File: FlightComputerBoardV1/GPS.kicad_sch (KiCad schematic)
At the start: 1 part

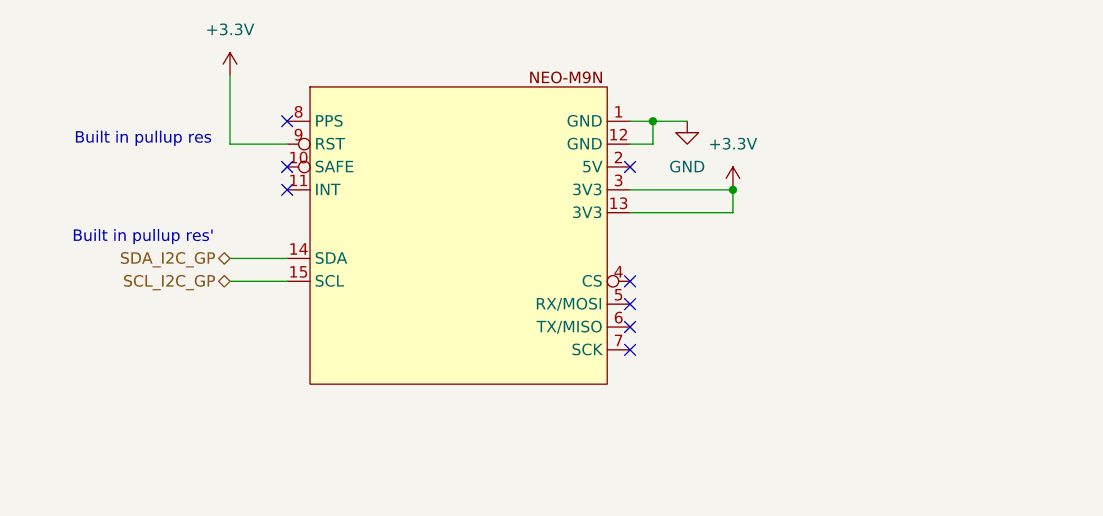
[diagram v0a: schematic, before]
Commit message: Test Points, BMP581
- Added I2C and other test points to schematic
- Added BMP581 symbol, footprint, and schematic on Peripherals sheet
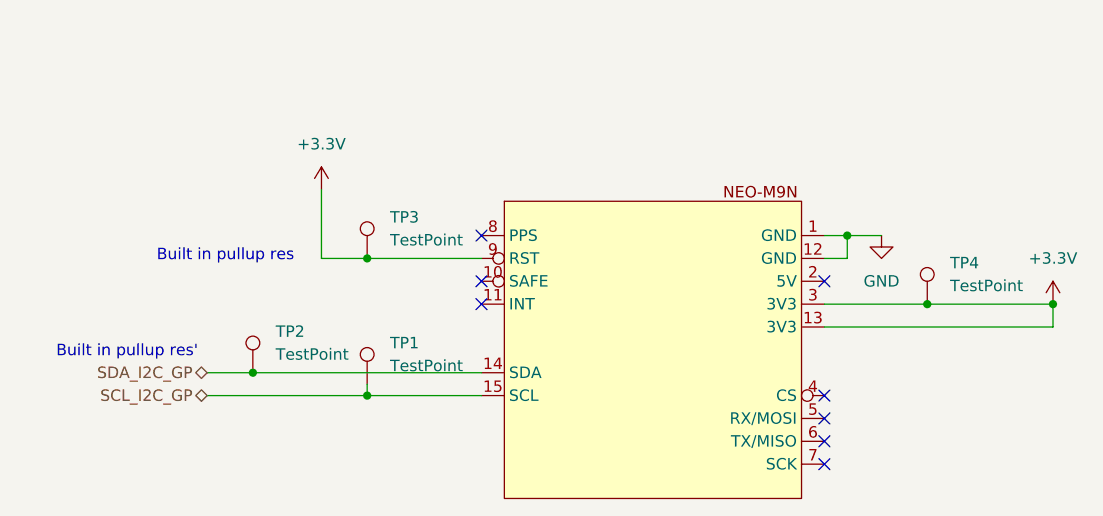
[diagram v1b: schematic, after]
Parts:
- added TP1, TP2, TP3, TP4: TestPoint, symbol Connector:TestPoint
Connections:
- net +3.3V: now also TP3.1, TP4.1
- net SCL_I2C_GP: now also TP1.1
- net SDA_I2C_GP: now also TP2.1

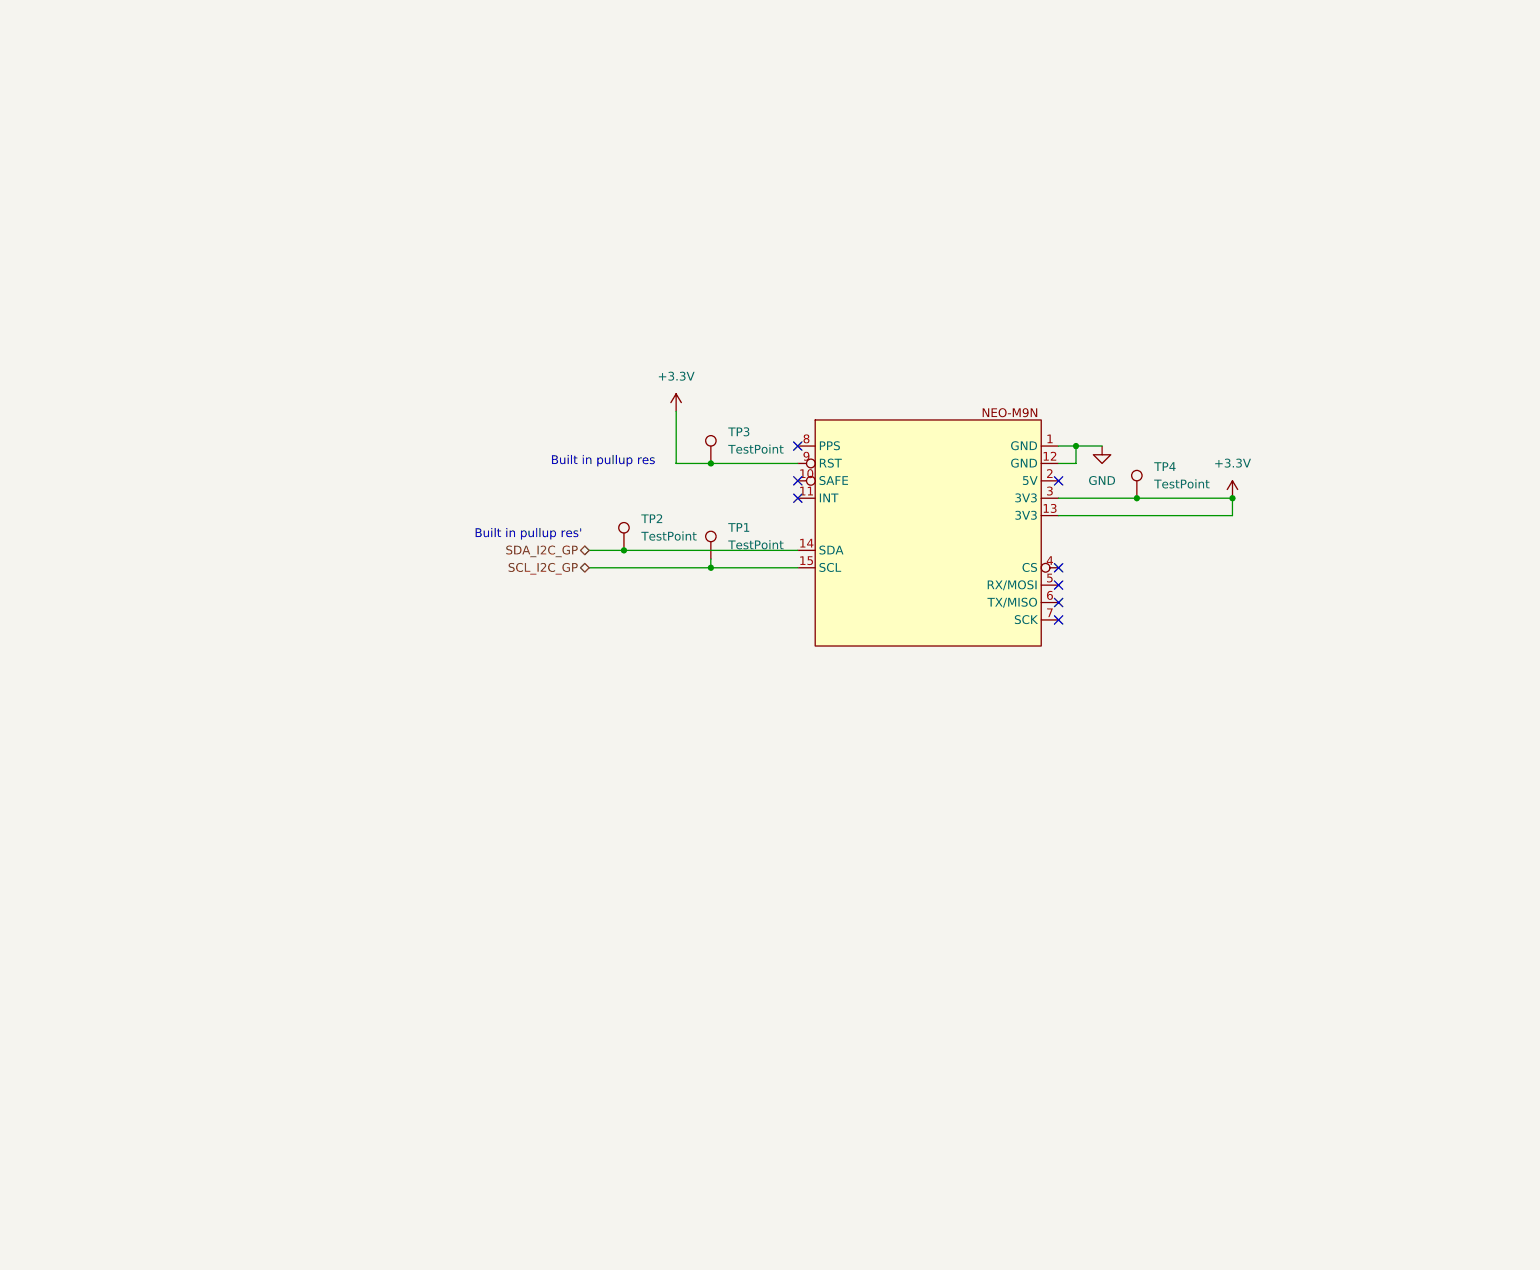
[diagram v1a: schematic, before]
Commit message: Late night shenanigans
- Added radar module sheet
- Created symbols for: radar, RFD900xus
- Added RFD900xus
- Fixed PT voltage dividers
To do:
- Add decoupling and test points
- Finish finding appropriate gate driver for H bridge linear actuator circuit
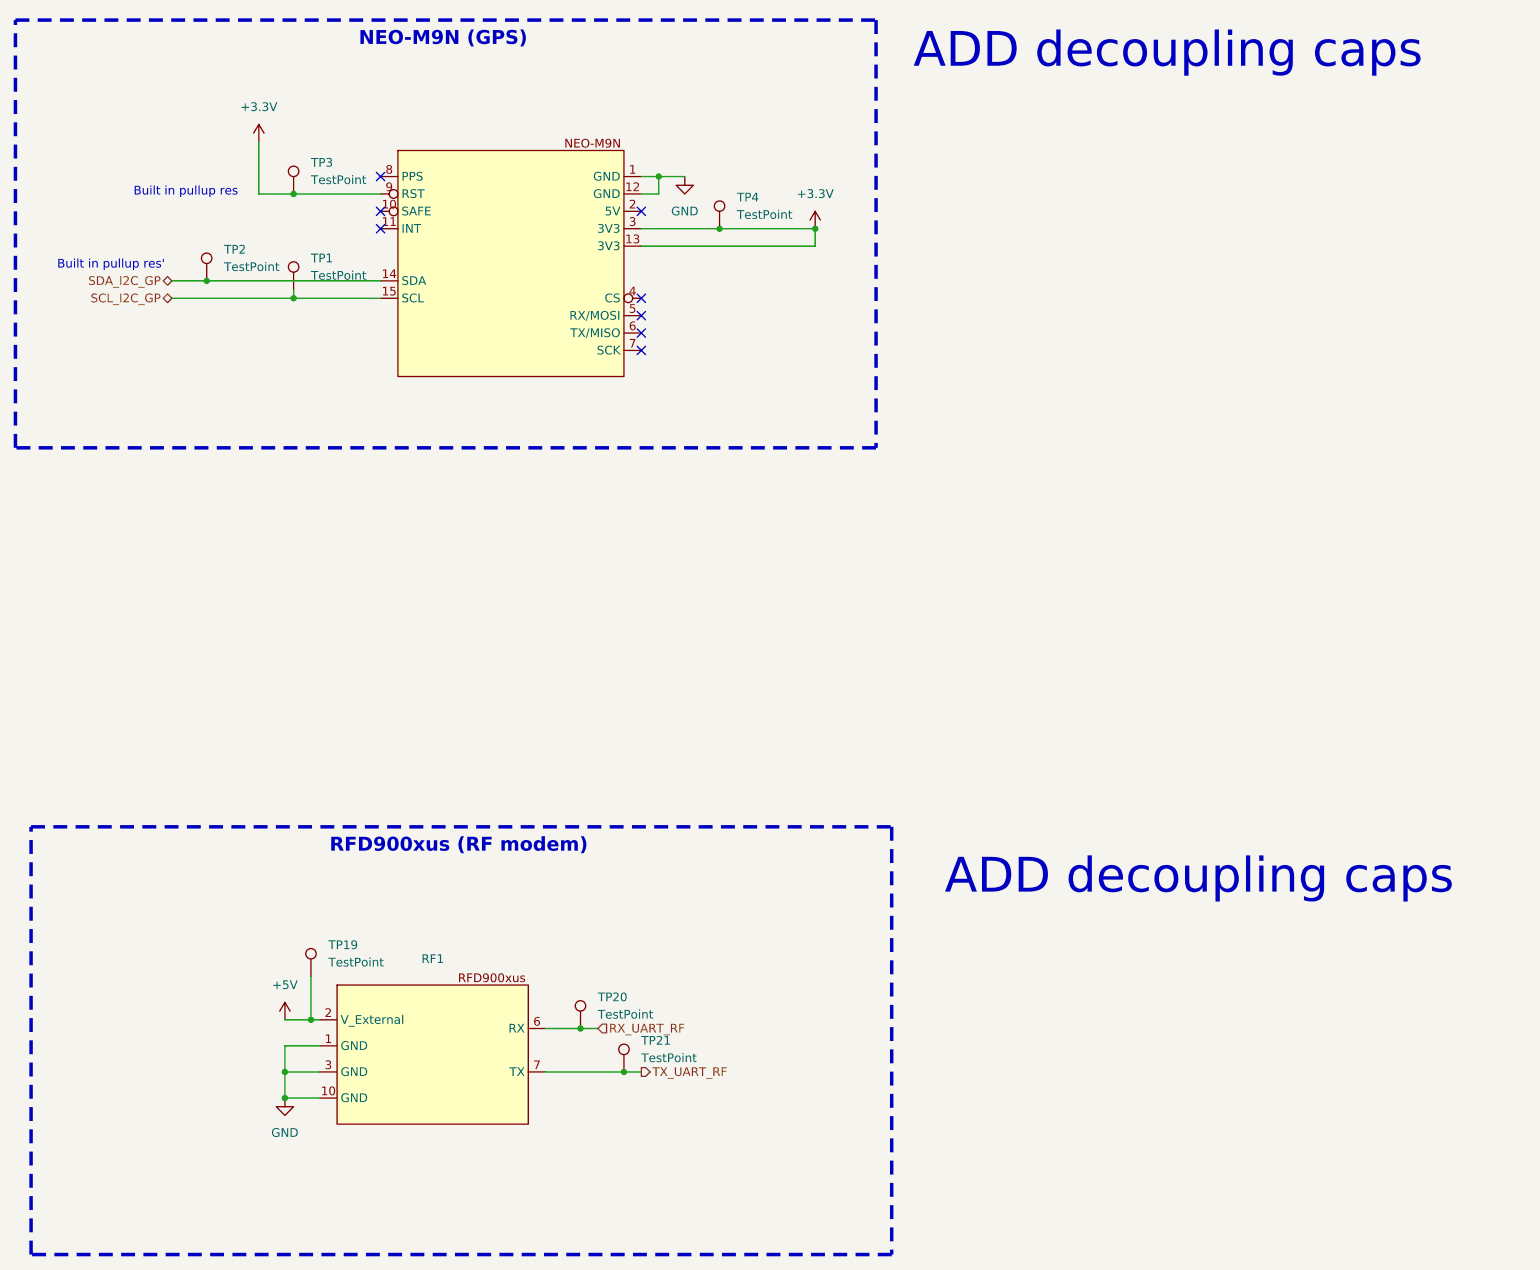
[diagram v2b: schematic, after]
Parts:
- added RF1: (no value), symbol FlightComputerBoardV1_Symbols:RFD900xus
- added TP19, TP20, TP21: TestPoint, symbol Connector:TestPoint
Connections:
- net GND: now also RF1.1 (GND), RF1.10 (GND), RF1.3 (GND)
- new net +5V: RF1.2 (V_External), TP19.1
- new net RX_UART_RF: RF1.6 (RX), TP20.1
- new net TX_UART_RF: RF1.7 (TX), TP21.1
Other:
- note added: "ADD decoupling caps"
- note added: "NEO-M9N (GPS)"
- note added: "RFD900xus (RF modem)"
- moved on the sheet: TP1, TP2, TP3, TP4
